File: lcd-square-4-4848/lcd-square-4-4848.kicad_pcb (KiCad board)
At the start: 2 copper layers, 73.5 x 68 mm, 54 parts, among them J1 SWD, J2 Conn_01x40_MountingPin, J3 Micro_SD_Card_Det1, J4 USB_C_Receptacle_USB2.0_16P, J5 Conn_01x02_MountingPin, SW1 BOOT0, SW2 RST, U1 MAX98357A, U2 TPS61169, U3 siplex-som-s16

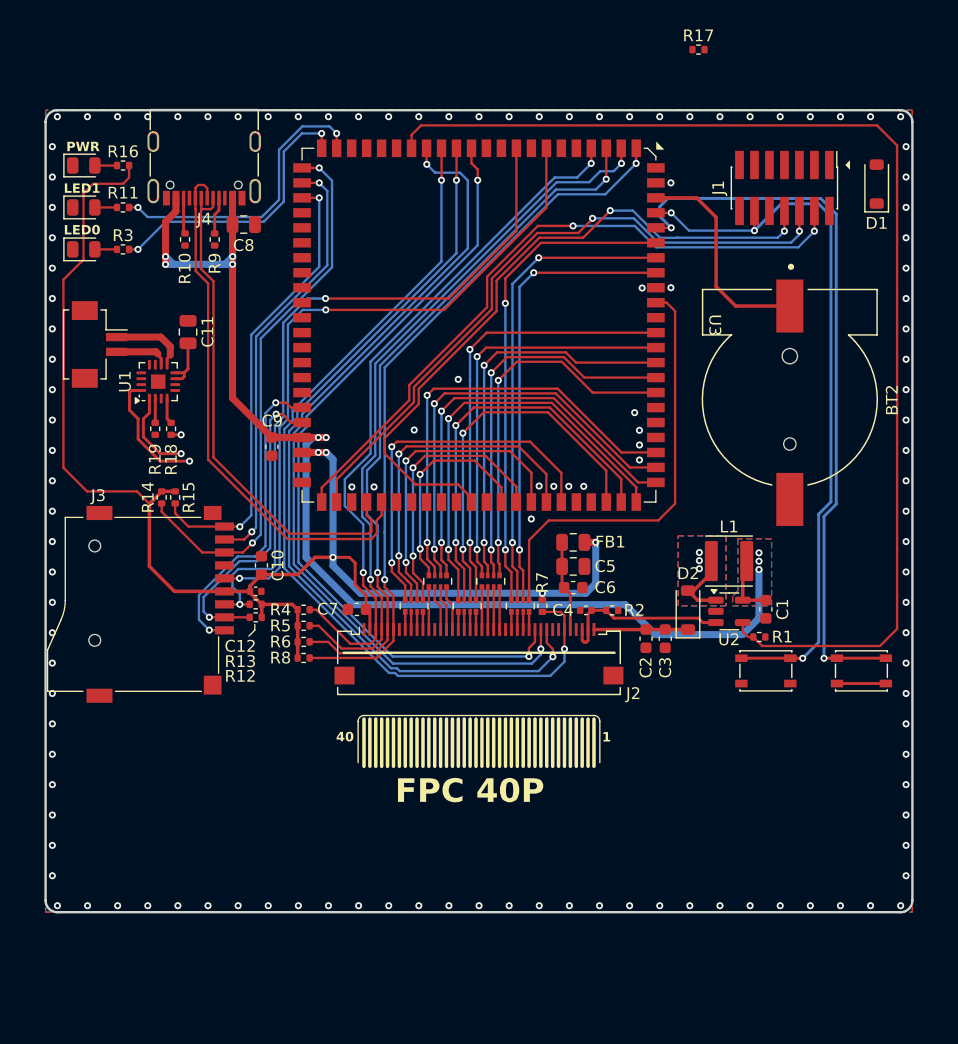
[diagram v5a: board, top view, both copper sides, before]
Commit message: Add LCD standard 7inch
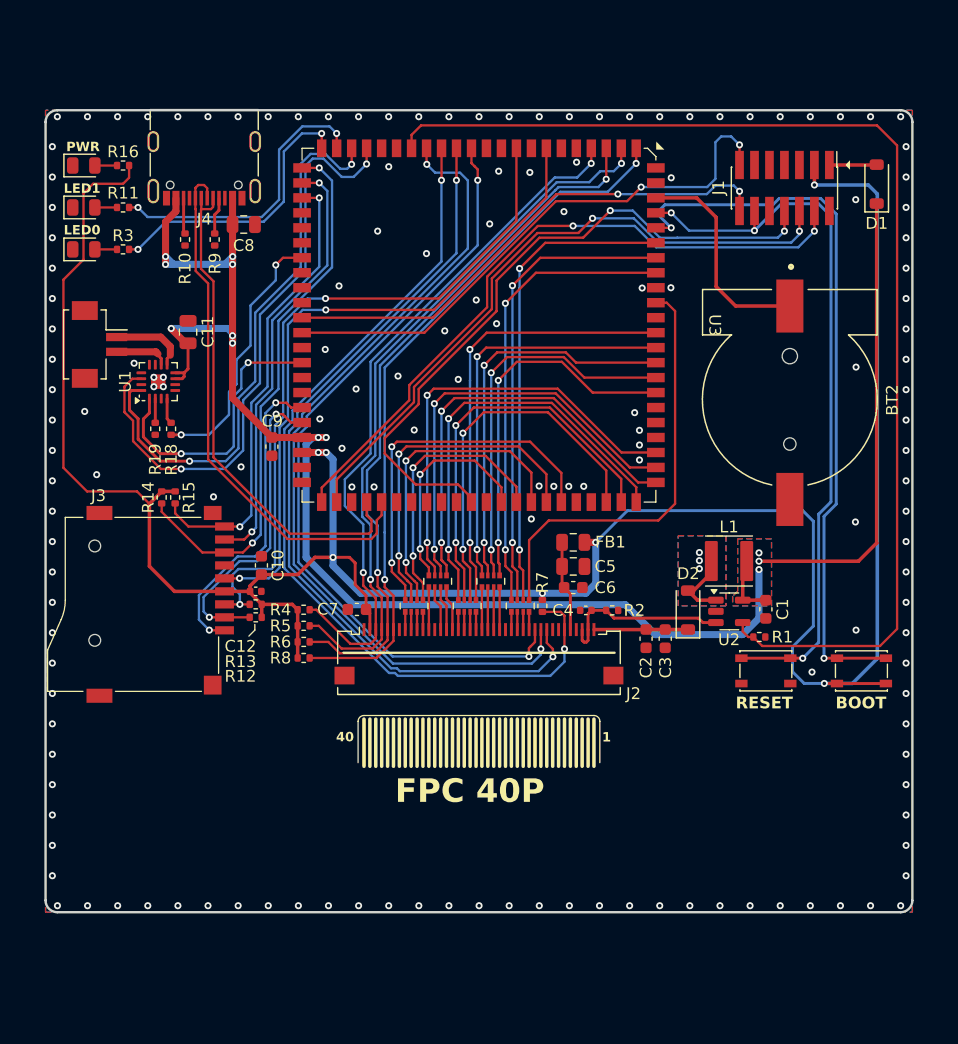
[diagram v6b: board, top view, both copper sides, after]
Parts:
- removed R17: 100, Resistor_SMD:R_0402_1005Metric
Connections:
- D1 pad 1: +5V -> VBUS
- J1 pad 11: Net-(J1-Pin_11) -> unconnected-(J1-Pin_11-Pad11)
- U3 pad 19: unconnected-(U3-PB12-Pad19) -> /I2S_WS
- U3 pad 20: unconnected-(U3-PB10-Pad20) -> /I2S_SCLK
- U3 pad 29: unconnected-(U3-PC8-Pad29) -> /~{SD_MODE}
- U3 pad 33: unconnected-(U3-PD5-Pad33) -> /VCP_TX
- U3 pad 34: unconnected-(U3-PD6-Pad34) -> /VCP_RX
- U3 pad 36: unconnected-(U3-PI3-Pad36) -> /I2S_SDO
- U3 pad 81: Net-(RN4-R3.2) -> Net-(RN4-R1.2)
- U3 pad 83: Net-(RN4-R1.2) -> Net-(RN4-R3.2)
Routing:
- net +3V3: track 127.3 -> 217.0 mm, vias 5 -> 7
- net /I2S_WS: track 0.00 -> 51.8 mm, vias 0 -> 2
- net /VCP_RX: track 0.00 -> 47.8 mm, vias 0 -> 2
- net VBUS: track 108.7 -> 156.3 mm, vias 9 -> 12
- net /VCP_TX: track 0.00 -> 43.6 mm, vias 0 -> 2
- net /I2S_SCLK: track 10.5 -> 48.1 mm, vias 1 -> 2
- net /~{SD_MODE}: track 0.85 -> 22.4 mm, vias 1 -> 2
- net /I2S_SDO: track 7.25 -> 24.1 mm, vias 1 -> 2
- net Net-(D1-A): track 0.00 -> 4.03 mm
- net Net-(RN4-R1.2): track 41.5 -> 39.2 mm
- net Net-(RN4-R3.2): track 38.7 -> 40.7 mm
- net /CMD: track 59.7 -> 59.2 mm
- net /CLK: track 57.0 -> 56.5 mm
- net GND: vias 124 -> 155
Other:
- board text added: "BOOT"
- board text added: "RESET"

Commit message: Slight changes
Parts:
- C1: footprint Capacitor_SMD:C_0603_1608Metric -> Capacitor_SMD:C_0805_2012Metric
- C6, C7, C9: footprint Capacitor_SMD:C_0603_1608Metric -> Capacitor_SMD:C_0402_1005Metric
- L1: value 6.8u -> 4.7u
- R2: footprint Resistor_SMD:R_0402_1005Metric -> Resistor_SMD:R_0603_1608Metric
- moved C1 1.41 mm to (169.8, 100.1), turned to 0 degrees
- moved R2 1.41 mm to (157.0, 100.5), turned to 90 degrees
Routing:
- net /SWO: track 57.6 -> 54.4 mm
- net VBUS: track 156.3 -> 154.5 mm
- net GND: vias 155 -> 163

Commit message: Rebuild 4inch LCD with non SOM
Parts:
- D3, D4: value LED -> RED
- D5: value LED -> GREEN
- RN1, RN2, RN3, RN4, RN5: value 22 -> 100
